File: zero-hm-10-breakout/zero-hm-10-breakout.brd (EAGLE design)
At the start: 25.1 x 34.3 mm, 9 parts, among them U1 HM-10

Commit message: final sent to oshpark.  tag it and bag it.
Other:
- board size 25.1 x 34.3 mm -> 25.4 x 34.3 mm
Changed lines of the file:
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@@
 <layer number="44" name="Drills" color="7" fill="1" visible="no" active="yes"/>
 <layer number="45" name="Holes" color="7" fill="1" visible="no" active="yes"/>
-<layer number="46" name="Milling" color="3" fill="1" visible="no" active="yes"/>
+<layer number="46" name="Milling" color="3" fill="1" visible="yes" active="yes"/>
 <layer number="47" name="Measures" color="7" fill="1" visible="no" active="yes"/>
 <layer number="48" name="Document" color="7" fill="1" visible="yes" active="yes"/>
@@
 <board>
 <plain>
-<wire x1="0" y1="0" x2="25.07" y2="0" width="0" layer="20"/>
-<wire x1="25.07" y1="0" x2="25.07" y2="27.93" width="0" layer="20"/>
-<wire x1="25.07" y1="27.93" x2="17.78" y2="34.28" width="0" layer="20"/>
-<wire x1="17.78" y1="34.29" x2="7.62" y2="34.29" width="0" layer="20"/>
-<wire x1="7.62" y1="34.29" x2="0" y2="27.94" width="0" layer="20"/>
-<wire x1="0" y1="27.93" x2="0" y2="0" width="0" layer="20"/>
-<text x="21.59" y="6.35" size="1.016" layer="21" rot="R90">Micah Pearlman -- Zero Engineering</text>
-<text x="3.81" y="26.67" size="1.016" layer="21" rot="R270">HM-10 XBee Breakout v1.0</text>
+<text x="21.59" y="1.27" size="1.016" layer="21" rot="R90">Micah Pearlman -- Zero Engineering</text>
+<text x="3.81" y="21.59" size="1.016" layer="21" rot="R270">HM-10 XBee Breakout v1.0</text>
+<wire x1="0" y1="27.94" x2="7.62" y2="34.29" width="0.4064" layer="20"/>
+<wire x1="7.62" y1="34.29" x2="17.78" y2="34.29" width="0.4064" layer="20"/>
+<wire x1="17.78" y1="34.29" x2="25.4" y2="27.94" width="0.4064" layer="20"/>
+<wire x1="25.4" y1="27.94" x2="25.4" y2="0" width="0.4064" layer="20"/>
+<wire x1="25.4" y1="0" x2="0" y2="0" width="0.4064" layer="20"/>
+<wire x1="0" y1="0" x2="0" y2="27.94" width="0.4064" layer="20"/>
+<wire x1="0" y1="27.94" x2="7.62" y2="34.29" width="0.4064" layer="46"/>
+<wire x1="7.62" y1="34.29" x2="17.78" y2="34.29" width="0.4064" layer="46"/>
+<wire x1="17.78" y1="34.29" x2="25.4" y2="27.94" width="0.4064" layer="46"/>
+<wire x1="25.4" y1="27.94" x2="25.4" y2="0" width="0.4064" layer="46"/>
+<wire x1="25.4" y1="0" x2="0" y2="0" width="0.4064" layer="46"/>
+<wire x1="0" y1="0" x2="0" y2="27.94" width="0.4064" layer="46"/>
 </plain>
 <attributes>

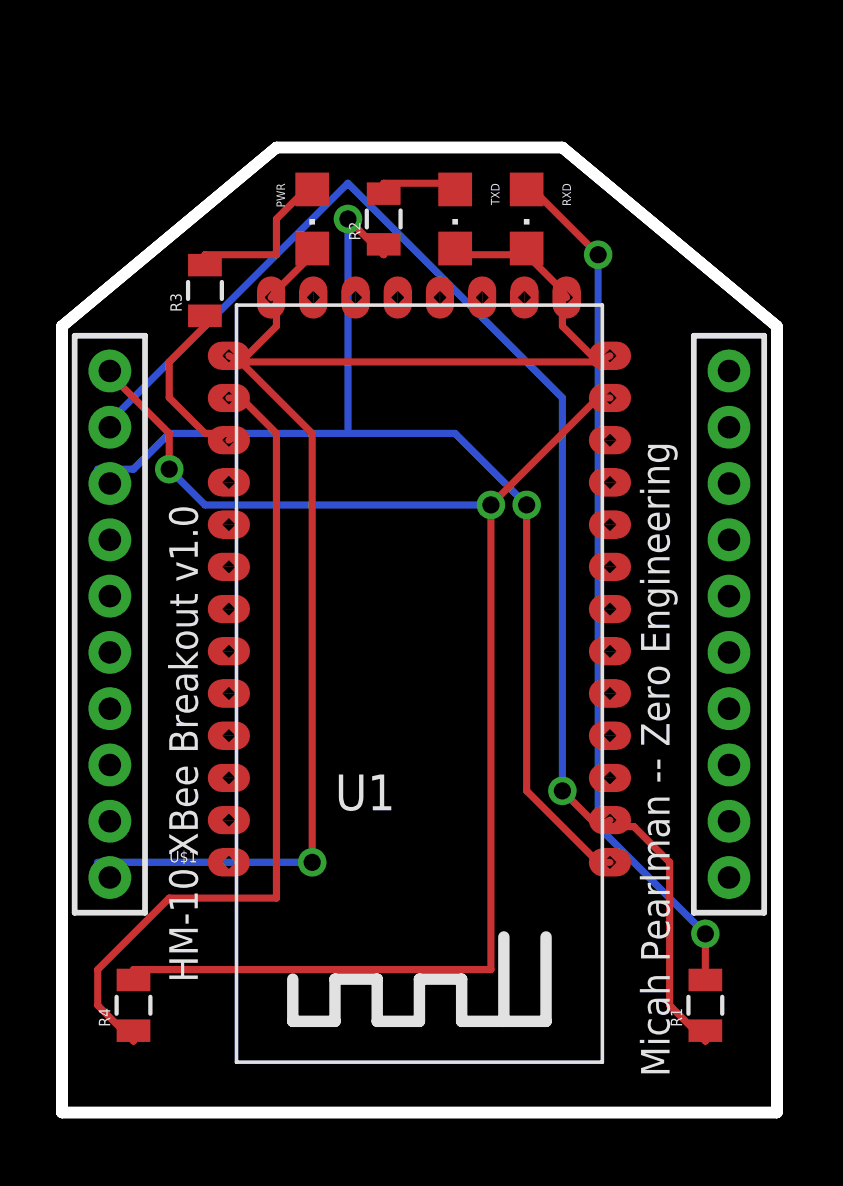
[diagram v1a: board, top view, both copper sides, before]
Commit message: added missing capacitor
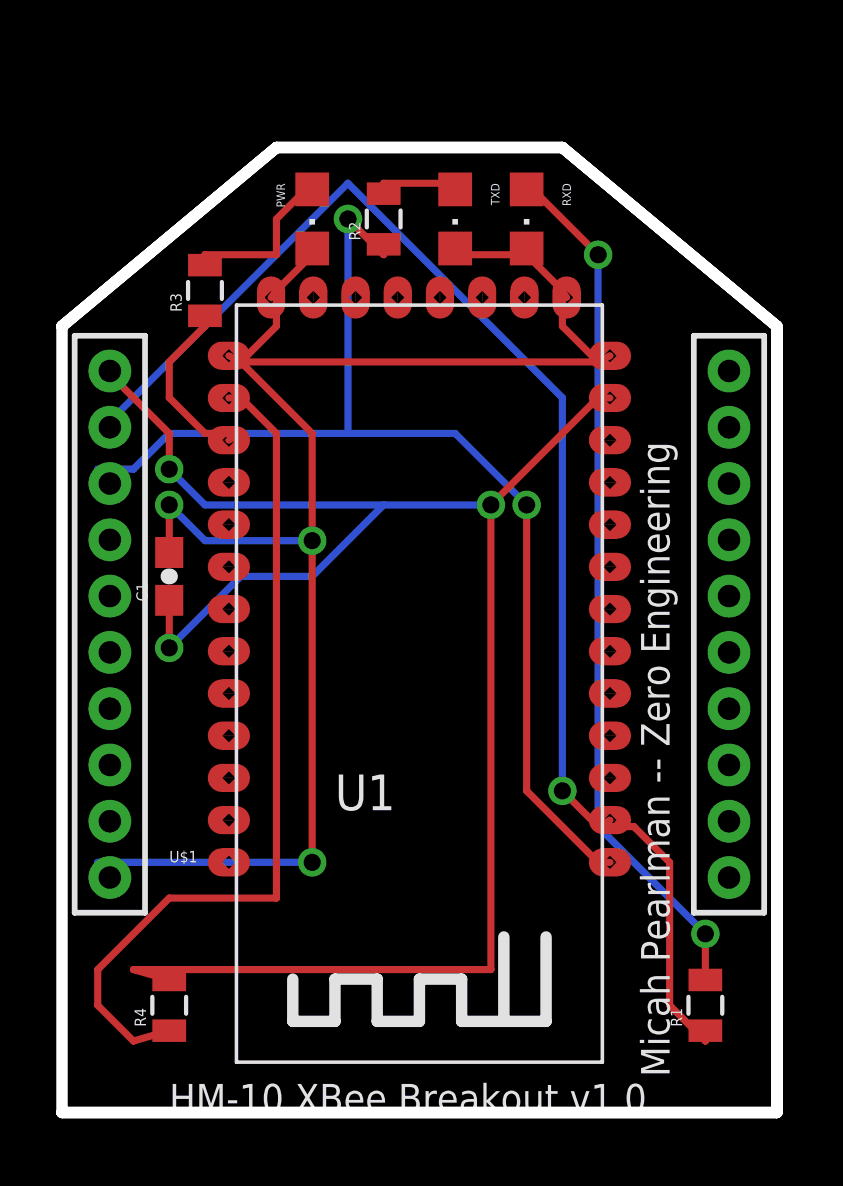
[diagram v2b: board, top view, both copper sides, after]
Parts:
- added C1: 0.1uF, SparkFun-Capacitors:0603-CAP
- moved R4 1.27 mm to (3.81, 3.81)
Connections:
- net GND: now also C1.2
- net VDD: now also C1.1
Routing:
- net VDD: track 52.7 -> 65.1 mm, vias 2 -> 3
- net GND: track 54.3 -> 61.6 mm, vias 1 -> 3
- net N$5: track 29.6 -> 30.5 mm
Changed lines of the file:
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@@
 <plain>
 <text x="21.59" y="1.27" size="1.016" layer="21" rot="R90">Micah Pearlman -- Zero Engineering</text>
-<text x="3.81" y="21.59" size="1.016" layer="21" rot="R270">HM-10 XBee Breakout v1.0</text>
+<text x="3.81" y="0" size="1.016" layer="21">HM-10 XBee Breakout v1.0</text>
 <wire x1="0" y1="27.94" x2="7.62" y2="34.29" width="0.4064" layer="20"/>
 <wire x1="7.62" y1="34.29" x2="17.78" y2="34.29" width="0.4064" layer="20"/>
@@
 <wire x1="25.4" y1="27.94" x2="25.4" y2="0" width="0.4064" layer="46"/>
 <wire x1="25.4" y1="0" x2="0" y2="0" width="0.4064" layer="46"/>
-<wire x1="0" y1="0" x2="0" y2="27.94" width="0.4064" layer="46"/>
 </plain>
 <attributes>
@@
 <attribute name="PROD_ID" value="RES-11622" x="43.18" y="68.58" size="1.778" layer="27" rot="R90" display="off"/>
 </element>
-<element name="R4" library="SparkFun-Resistors" package="0805" value="470R" x="2.54" y="3.81" rot="R90">
-<attribute name="PROD_ID" value="RES-11622" x="40.64" y="46.99" size="1.778" layer="27" rot="R90" display="off"/>
+<element name="R4" library="SparkFun-Resistors" package="0805" value="470R" x="3.81" y="3.81" rot="R90">
+<attribute name="PROD_ID" value="RES-11622" x="41.91" y="46.99" size="1.778" layer="27" rot="R90" display="off"/>
 </element>
 <element name="RXD" library="adafruit" package="CHIPLED_0805" value="GRN" x="16.51" y="31.75" smashed="yes" rot="R180">
@@
 <attribute name="NAME" x="7.62" y="33.02" size="0.3048" layer="25" rot="R270"/>
 <attribute name="VALUE" x="10.16" y="33.02" size="0.3048" layer="27" rot="R270"/>
+</element>
+<element name="C1" library="SparkFun-Capacitors" package="0603-CAP" value="0.1uF" x="3.81" y="19.05" rot="R90">
+<attribute name="PROD_ID" value="CAP-00810" x="3.81" y="19.05" size="1.27" layer="27" rot="R90" display="off"/>
 </element>
 </elements>
@@
 <wire x1="7.62" y1="29.21" x2="7.43" y2="28.96" width="0.254" layer="1"/>
 <wire x1="8.89" y1="8.89" x2="1.27" y2="8.89" width="0.254" layer="16"/>
-<wire x1="8.89" y1="24.13" x2="8.89" y2="8.89" width="0.254" layer="1"/>
+<wire x1="8.89" y1="24.13" x2="8.89" y2="20.32" width="0.254" layer="1"/>
+<wire x1="8.89" y1="20.32" x2="8.89" y2="8.89" width="0.254" layer="1"/>
 <wire x1="6.35" y1="26.67" x2="8.89" y2="24.13" width="0.254" layer="1"/>
 <wire x1="1.27" y1="8.89" x2="1.7" y2="8.35" width="0.254" layer="16"/>
@@
 <wire x1="6.35" y1="26.67" x2="5.93" y2="26.89" width="0.254" layer="1"/>
 <via x="8.89" y="8.89" extent="1-16" drill="0.6096"/>
+<contactref element="C1" pad="2"/>
+<wire x1="3.81" y1="21.59" x2="3.81" y2="19.9" width="0.254" layer="1"/>
+<wire x1="5.08" y1="20.32" x2="3.81" y2="21.59" width="0.254" layer="16"/>
+<wire x1="8.89" y1="20.32" x2="5.08" y2="20.32" width="0.254" layer="16"/>
+<via x="3.81" y="21.59" extent="1-16" drill="0.6096"/>
+<via x="8.89" y="20.32" extent="1-16" drill="0.6096"/>
 </signal>
 <signal name="VDD">
@@
 <wire x1="15.24" y1="21.59" x2="15.24" y2="5.08" width="0.254" layer="1"/>
 <wire x1="19.05" y1="25.4" x2="15.24" y2="21.59" width="0.254" layer="1"/>
-<wire x1="2.54" y1="5.08" x2="2.54" y2="4.71" width="0.254" layer="1"/>
+<wire x1="2.54" y1="5.08" x2="3.81" y2="4.71" width="0.254" layer="1"/>
 <wire x1="19.05" y1="25.4" x2="19.47" y2="25.39" width="0.254" layer="1"/>
 <wire x1="3.81" y1="24.13" x2="1.27" y2="26.67" width="0.254" layer="1"/>
 <wire x1="3.81" y1="22.86" x2="3.81" y2="24.13" width="0.254" layer="1"/>
 <wire x1="5.08" y1="21.59" x2="3.81" y2="22.86" width="0.254" layer="16"/>
-<wire x1="15.24" y1="21.59" x2="5.08" y2="21.59" width="0.254" layer="16"/>
+<wire x1="15.24" y1="21.59" x2="11.43" y2="21.59" width="0.254" layer="16"/>
+<wire x1="11.43" y1="21.59" x2="5.08" y2="21.59" width="0.254" layer="16"/>
 <wire x1="1.27" y1="26.67" x2="1.7" y2="26.35" width="0.254" layer="1"/>
 <via x="3.81" y="22.86" extent="1-16" drill="0.6096"/>
 <via x="15.24" y="21.59" extent="1-16" drill="0.6096"/>
+<contactref element="C1" pad="1"/>
+<wire x1="3.81" y1="16.51" x2="3.81" y2="18.2" width="0.254" layer="1"/>
+<wire x1="6.35" y1="19.05" x2="3.81" y2="16.51" width="0.254" layer="16"/>
+<wire x1="8.89" y1="19.05" x2="6.35" y2="19.05" width="0.254" layer="16"/>
+<wire x1="11.43" y1="21.59" x2="8.89" y2="19.05" width="0.254" layer="16"/>
+<via x="3.81" y="16.51" extent="1-16" drill="0.6096"/>
 </signal>
 <signal name="TX">
@@
 <wire x1="7.62" y1="24.13" x2="7.62" y2="7.62" width="0.254" layer="1"/>
 <wire x1="6.35" y1="25.4" x2="7.62" y2="24.13" width="0.254" layer="1"/>
-<wire x1="2.54" y1="2.54" x2="2.54" y2="2.91" width="0.254" layer="1"/>
+<wire x1="2.54" y1="2.54" x2="3.81" y2="2.91" width="0.254" layer="1"/>
 <wire x1="6.35" y1="25.4" x2="5.93" y2="25.39" width="0.254" layer="1"/>
 </signal>

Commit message: Fixed RX/TX being backwards and removed the RX/TX LEDs
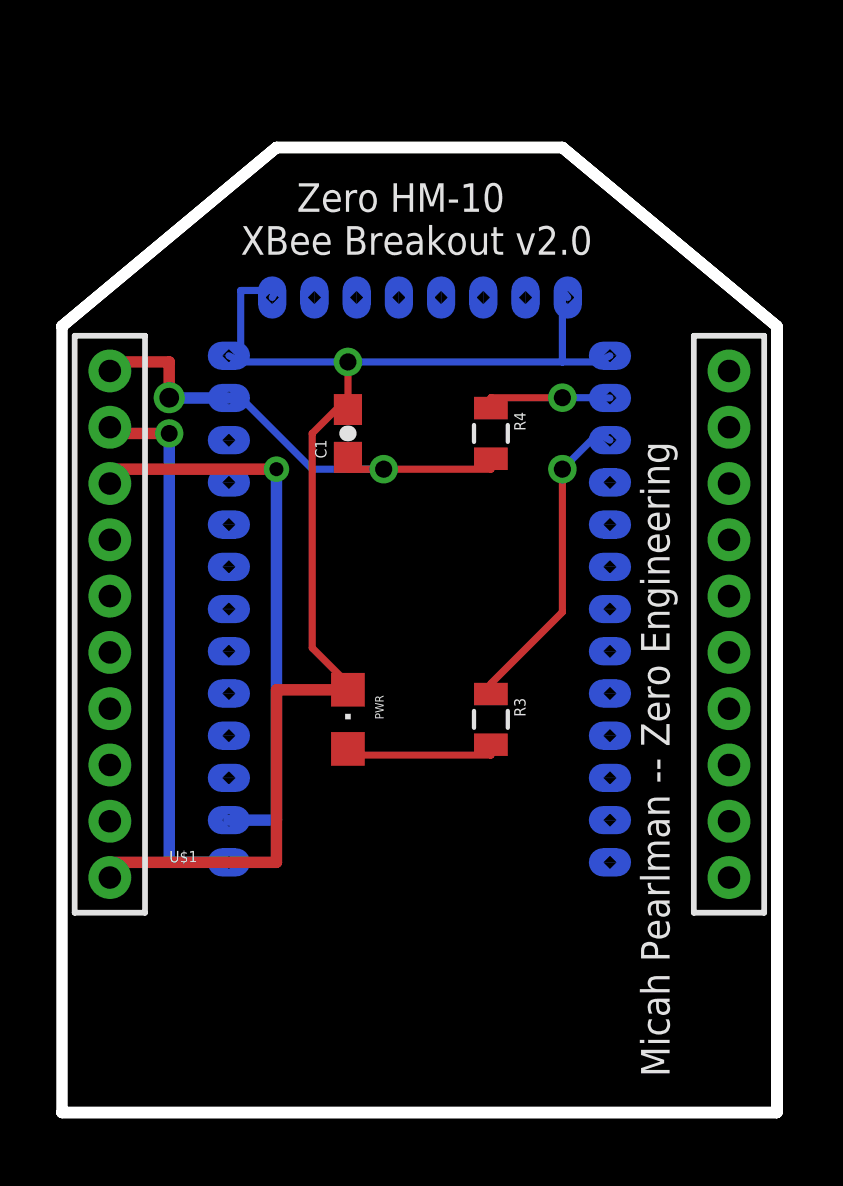
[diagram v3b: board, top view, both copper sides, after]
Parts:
- removed R1, R2: 470R, SparkFun-Resistors:0805
- removed RXD: GRN, adafruit:CHIPLED_0805
- removed TXD: RED, adafruit:CHIPLED_0805
- moved R4 23.3 mm to (15.2, 24.1), turned to 270 degrees
- moved R3 18.3 mm to (15.2, 14.0), turned to 270 degrees
- moved PWR 17.8 mm to (10.2, 14.0), turned to 0 degrees
- moved C1 8.13 mm to (10.2, 24.1)
- flipped U1 to the bottom
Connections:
- removed net N$1: R2.2, TXD.A
- removed net N$2: R1.2, RXD.A
- net GND: no longer RXD.C, TXD.C
- net RX: now also U1.1; no longer R1.1, U1.2
- net TX: now also U1.2; no longer R2.1, U1.1
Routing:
- net VDD: track 65.1 -> 18.3 mm, vias 3 -> 2
- net N$2: track 31.2 -> 0.00 mm, vias 2 -> 0
- net RX: track 50.4 -> 19.7 mm
- net N$5: track 30.5 -> 4.60 mm, vias 0 -> 1
- net TX: track 41.4 -> 20.6 mm, vias 2 -> 1
- net GND: track 61.6 -> 48.9 mm, vias 3 -> 1
- net N$4: track 6.99 -> 11.3 mm, vias 0 -> 1
- net N$1: track 3.13 -> 0.00 mm
- net N$3: track 6.20 -> 5.67 mm
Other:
- board text added: "Zero HM-10 XBee Breakout v2.0"
- board text removed: "HM-10 XBee Breakout v1.0"

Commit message: updated board and schematic images and parts list
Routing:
- net VDD: track 18.3 -> 19.5 mm
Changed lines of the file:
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@@
 <board>
 <plain>
-<text x="21.59" y="1.27" size="1.016" layer="21" rot="R90">Micah Pearlman -- Zero Engineering</text>
-<text x="6.35" y="30.48" size="1.016" layer="21">     Zero HM-10
+<text x="21.59" y="1.27" size="0.8128" layer="21" font="fixed" rot="R90">Micah Pearlman -- Zero Engineering</text>
+<text x="5.08" y="30.48" size="1.016" layer="21" font="fixed">   Zero HM-10
 XBee Breakout v2.0</text>
 <wire x1="0" y1="27.94" x2="7.62" y2="34.29" width="0.4064" layer="20"/>
@@
 <contactref element="R4" pad="2"/>
 <contactref element="C1" pad="1"/>
-<wire x1="15.24" y1="22.86" x2="11.43" y2="22.86" width="0.254" layer="1"/>
-<wire x1="11.43" y1="22.86" x2="10.16" y2="22.86" width="0.254" layer="1"/>
+<wire x1="15.24" y1="22.86" x2="12.7" y2="22.86" width="0.254" layer="1"/>
+<wire x1="12.7" y1="22.86" x2="10.16" y2="22.86" width="0.254" layer="1"/>
 <wire x1="10.16" y1="22.86" x2="10.16" y2="23.28" width="0.254" layer="1"/>
 <wire x1="15.24" y1="22.86" x2="15.24" y2="23.23" width="0.254" layer="1"/>
 <wire x1="8.89" y1="22.86" x2="6.35" y2="25.4" width="0.254" layer="16"/>
-<wire x1="11.43" y1="22.86" x2="8.89" y2="22.86" width="0.254" layer="16"/>
+<wire x1="12.7" y1="22.86" x2="8.89" y2="22.86" width="0.254" layer="16"/>
 <wire x1="6.35" y1="25.4" x2="5.93" y2="25.39" width="0.254" layer="16"/>
-<via x="11.43" y="22.86" extent="1-16" drill="0.6096"/>
+<via x="12.7" y="22.86" extent="1-16" drill="0.6096"/>
 <wire x1="5.93" y1="25.39" x2="3.81" y2="25.39" width="0.4064" layer="16"/>
-<wire x1="3.81" y1="25.39" x2="3.81" y2="25.4" width="0.4064" layer="16"/>
-<via x="3.81" y="25.4" extent="1-16" drill="0.7"/>
-<wire x1="3.81" y1="25.4" x2="3.81" y2="26.67" width="0.4064" layer="1"/>
+<wire x1="3.81" y1="25.39" x2="3.81" y2="26.67" width="0.4064" layer="16"/>
+<via x="3.81" y="26.67" extent="1-16" drill="0.7"/>
 <wire x1="3.81" y1="26.67" x2="1.7" y2="26.67" width="0.4064" layer="1"/>
 <wire x1="1.7" y1="26.67" x2="1.7" y2="26.35" width="0.4064" layer="1"/>
